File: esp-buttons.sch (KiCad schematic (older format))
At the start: 25 parts, among them Q1 FDV304P, U1 ESP-07v2, U2 LD1117S33CTR

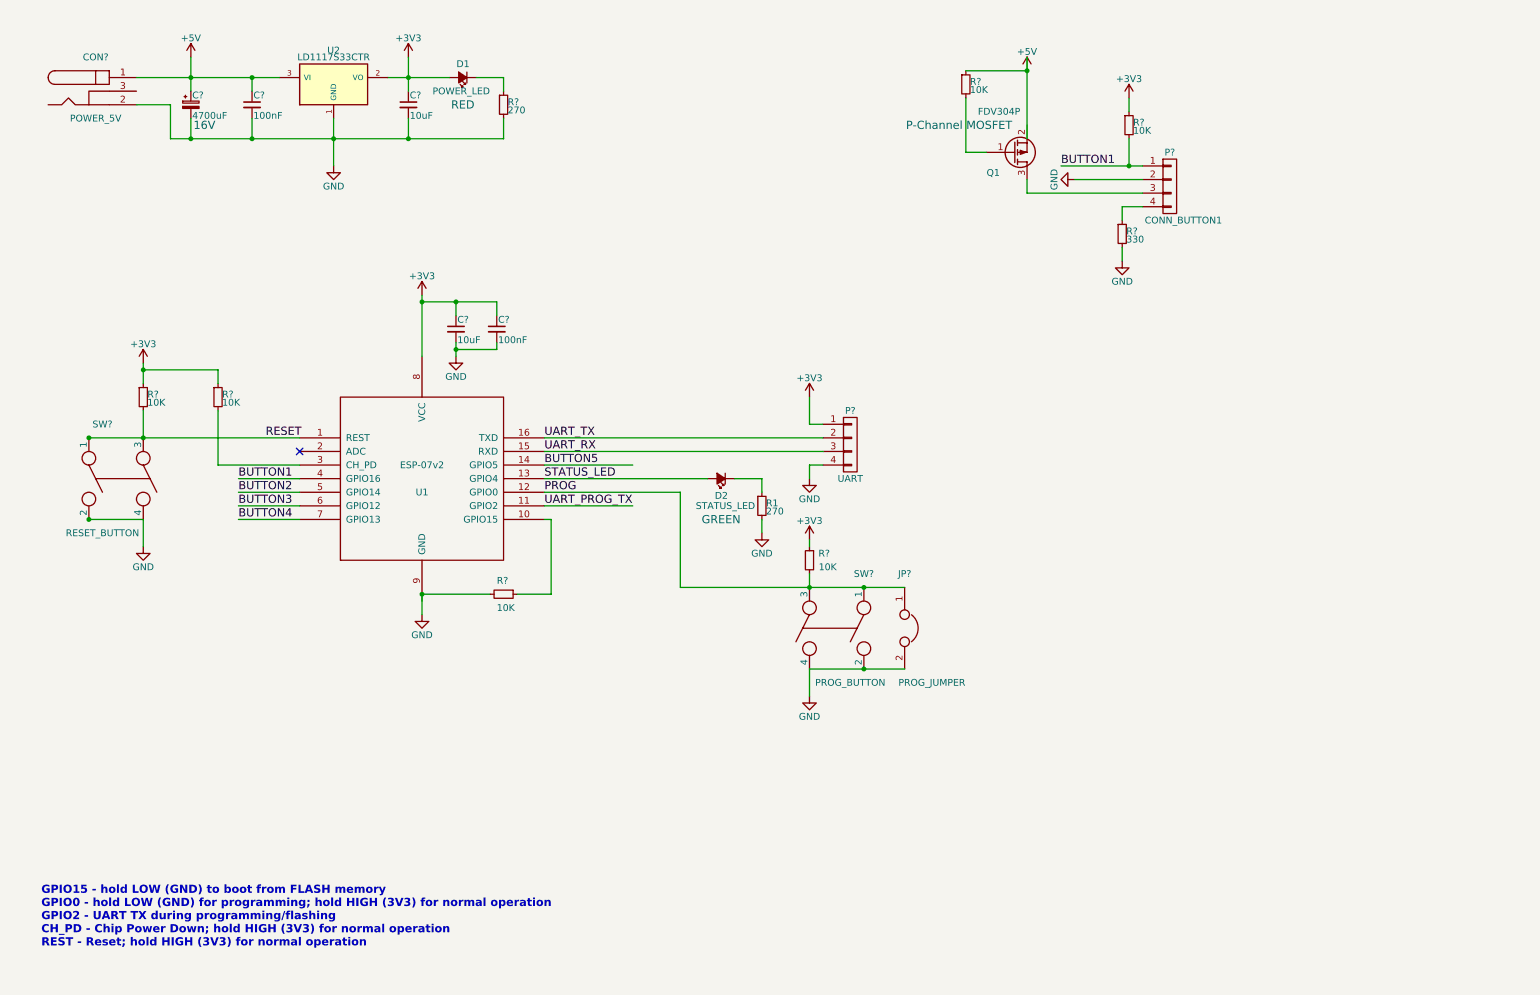
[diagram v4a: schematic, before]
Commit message: Added better circuit for BUTTON! & LED1
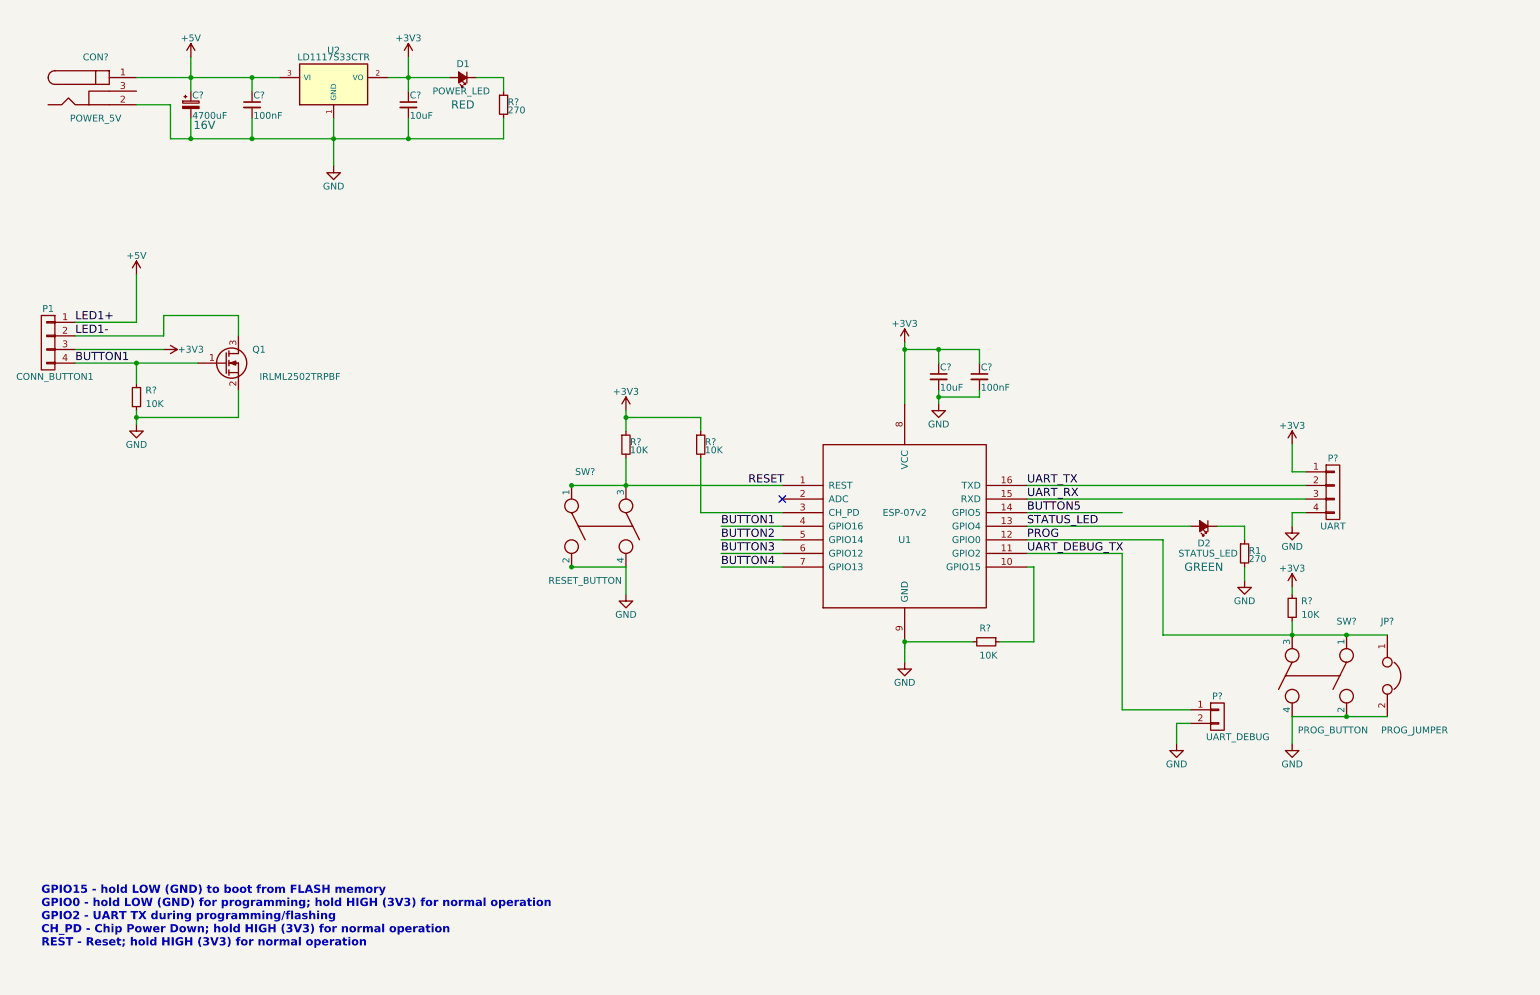
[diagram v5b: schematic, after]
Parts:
- removed Q1: FDV304P, TO_SOT_Packages_SMD:SOT-23, symbol Q_PMOS_GSD
- removed R?: 10K, Resistors_SMD:R_1206_HandSoldering, symbol R_Small
- removed R?: 330, Resistors_SMD:R_1206_HandSoldering, symbol R_Small
- added P?: UART_DEBUG, Pin_Headers:Pin_Header_Straight_1x02, symbol CONN_01X02
- added Q?: IRLML2502TRPBF, TO_SOT_Packages_SMD:SOT-23, symbol Q_NMOS_GSD
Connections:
- net labels added: LED1+, LED1-, UART_DEBUG_TX
- net labels removed: UART_PROG_TX
- wire segments 93 -> 75
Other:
- moved on the sheet: C?, D2, JP?, P1, P?, R1, R?, SW?, U1

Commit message: Added the rest of the buttons' circuits. Annotated the schematic
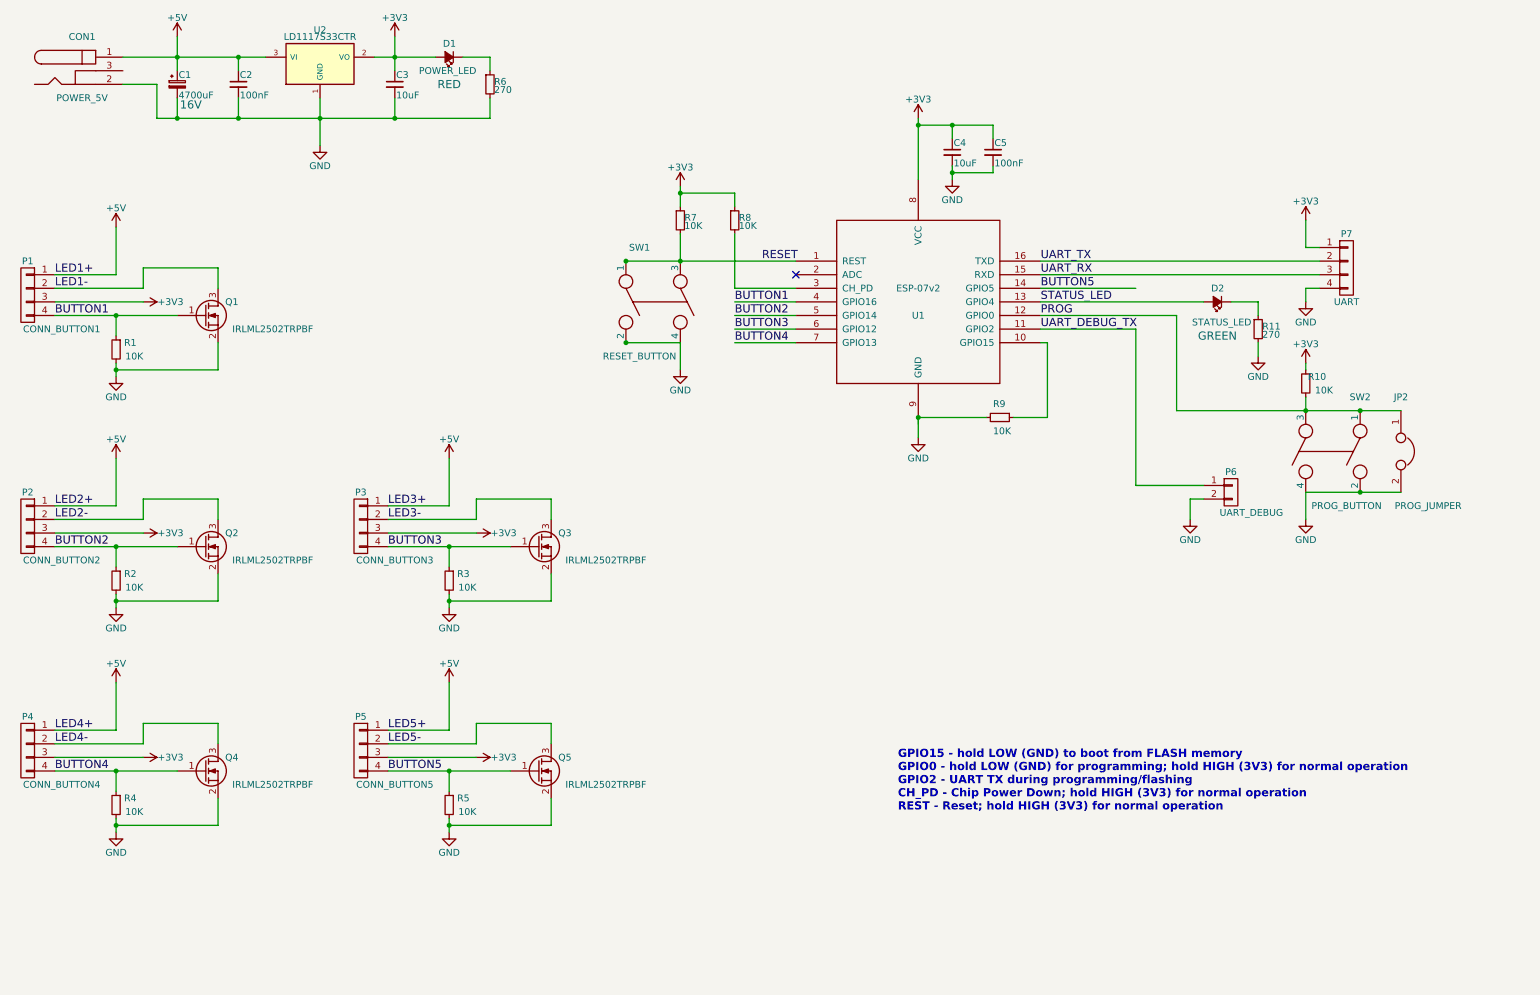
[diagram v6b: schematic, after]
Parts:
- added P2: CONN_BUTTON2, symbol CONN_01X04
- added P3: CONN_BUTTON3, symbol CONN_01X04
- added P4: CONN_BUTTON4, symbol CONN_01X04
- added P5: CONN_BUTTON5, symbol CONN_01X04
- added Q2, Q3, Q4, Q5: IRLML2502TRPBF, TO_SOT_Packages_SMD:SOT-23, symbol Q_NMOS_GSD
- added R2, R3, R4, R5: 10K, Resistors_SMD:R_1206_HandSoldering, symbol R_Small
- gave numbers to parts that had none: 19
- renumbered R1 to R11
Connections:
- net +3V3: now also P2.3 (P3), P3.3 (P3), P4.3 (P3), P5.3 (P3)
- net +5V: now also P2.1 (P1), P3.1 (P1), P4.1 (P1), P5.1 (P1)
- net BUTTON2: now also P2.4 (P4), Q2.1 (G), R2.1
- net BUTTON3: now also P3.4 (P4), Q3.1 (G), R3.1
- net BUTTON4: now also P4.4 (P4), Q4.1 (G), R4.1
- net BUTTON5: now also P5.4 (P4), Q5.1 (G), R5.1
- net GND: now also Q2.2 (S), Q3.2 (S), Q4.2 (S), Q5.2 (S), R2.2, R3.2, R4.2, R5.2
- new net LED2-: P2.2 (P2), Q2.3 (D)
- new net LED3-: P3.2 (P2), Q3.3 (D)
- new net LED4-: P4.2 (P2), Q4.3 (D)
- new net LED5-: P5.2 (P2), Q5.3 (D)
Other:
- moved on the sheet: C1, C2, C3, C4, C5, CON1, D1, D2, JP2, P1, P6, P7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

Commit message: Added circuit for USB-to-serial IC (FT230X). Added additional 5V power connector (terminal block connector)
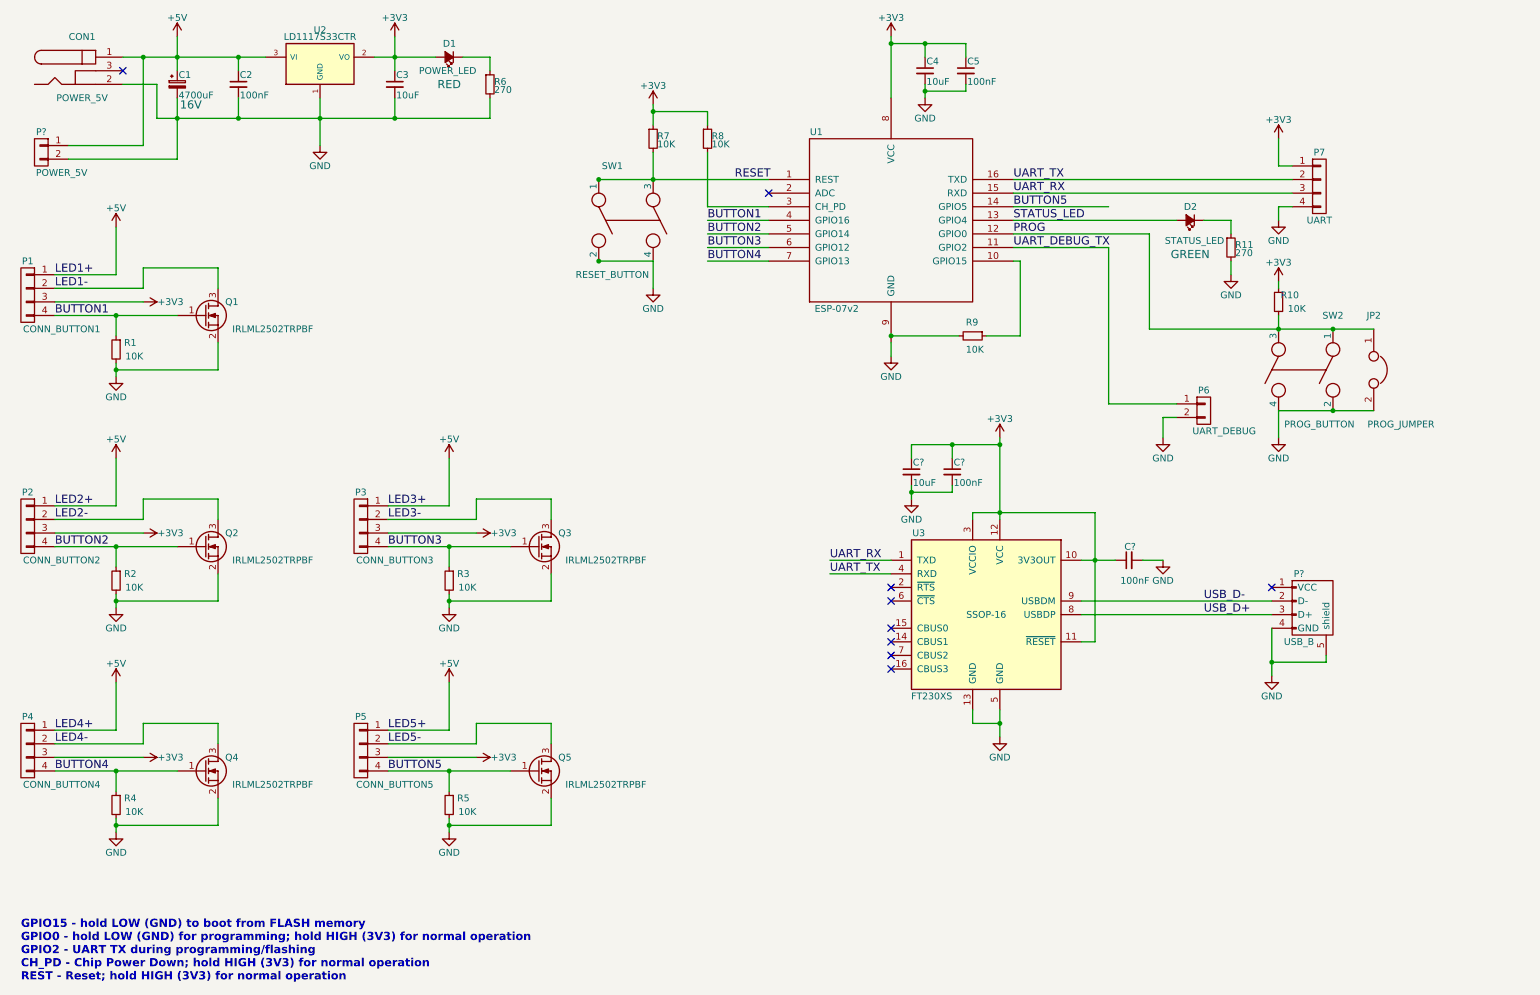
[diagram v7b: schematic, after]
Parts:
- added C?: 10uF, Capacitors_SMD:C_1210_HandSoldering, symbol C_Small
- added C? (x2): 100nF, Capacitors_SMD:C_1206_HandSoldering, symbol C_Small
- added P?: USB_B, Connect:USB_B, symbol USB_B
- added P?: POWER_5V, symbol CONN_01X02
- added U3: FT230XS, SSOP-16, symbol FT230XS
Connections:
- net +3V3: now also C?.1, C?.1, C?.1, U3.10 (3V3OUT), U3.11 (~RESET), U3.12 (VCC), U3.3 (VCCIO)
- net +5V: now also P?.1 (P1)
- net GND: now also U1.9 (GND), C?.2, C?.2, C?.2, P?.2 (P2), P?.4 (GND), P?.5 (shield), U3.13 (GND), U3.5 (GND); no longer R9.2
- net UART_RX: now also U3.1 (TXD)
- net UART_TX: now also U3.4 (RXD)
- new net USB_D+: P?.3 (D+), U3.8 (USBDP)
- new net USB_D-: P?.2 (D-), U3.9 (USBDM)
- no-connect marks 1 -> 9
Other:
- moved on the sheet: C4, C5, D2, JP2, P6, P7, R10, R11, R7, R8, R9, SW1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

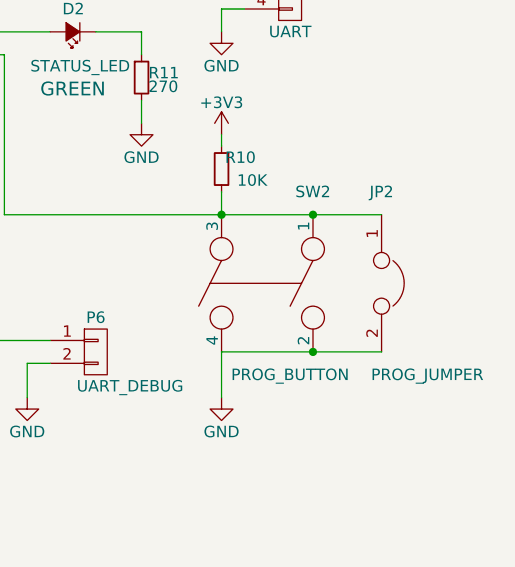
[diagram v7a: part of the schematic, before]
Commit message: Added temporary footprints to the button's connectors and the buttons
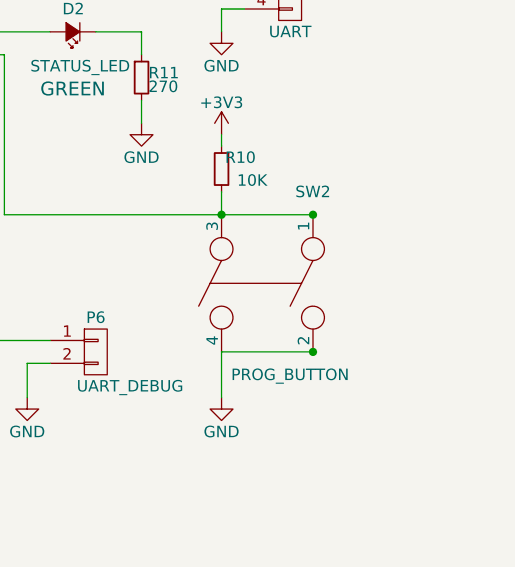
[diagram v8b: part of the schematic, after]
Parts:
- removed JP2: PROG_JUMPER, symbol JUMPER
- P1, P3, P4, P5: footprint (none) -> Terminal_Blocks:TerminalBlock_Pheonix_PT-3.5mm_4pol
- P2, P?: footprint (none) -> Terminal_Blocks:TerminalBlock_Pheonix_PT-3.5mm_2pol
- SW1: footprint (none) -> Buttons_Switches_SMD:SW_SPST_EVPBF
- SW2: footprint (none) -> Buttons_Switches_ThroughHole:SW_PUSH_6mm
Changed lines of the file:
@@
 F 0 "SW1" V 4600 2050 50  0000 C CNN
 F 1 "RESET_BUTTON" V 5400 2050 50  0000 C CNN
-F 2 "" H 5000 2150 50  0000 C CNN
+F 2 "Buttons_Switches_SMD:SW_SPST_EVPBF" H 5000 2150 50  0001 C CNN
 F 3 "" H 5000 2150 50  0000 C CNN
 	1    5000 2150
@@
 F 0 "P1" H 600 2950 50  0000 C CNN
 F 1 "CONN_BUTTON1" H 350 2450 50  0000 C CNN
-F 2 "" H 600 2700 50  0000 C CNN
+F 2 "Terminal_Blocks:TerminalBlock_Pheonix_PT-3.5mm_4pol" H 600 2700 50  0001 C CNN
 F 3 "" H 600 2700 50  0000 C CNN
 	1    600  2700
@@
 F 0 "SW2" V 9600 3050 50  0000 C CNN
 F 1 "PROG_BUTTON" V 10400 3150 50  0000 C CNN
-F 2 "" H 10000 3250 50  0000 C CNN
+F 2 "Buttons_Switches_ThroughHole:SW_PUSH_6mm" H 10000 3250 50  0001 C CNN
 F 3 "" H 10000 3250 50  0000 C CNN
 	1    10000 3250
@@
 Text Label 7850 2250 0    60   ~ 0
 PROG
-$Comp
-L JUMPER JP2
-U 1 1 57C84572
-P 10500 3250
-F 0 "JP2" V 10100 3250 50  0000 C CNN
-F 1 "PROG_JUMPER" V 10900 3450 50  0000 C CNN
-F 2 "" H 10500 3250 50  0000 C CNN
-F 3 "" H 10500 3250 50  0000 C CNN
-	1    10500 3250
-	0    1    1    0
-$EndComp
 Text Label 7850 2050 0    60   ~ 0
 BUTTON5
@@
 F 0 "P2" H 600 4650 50  0000 C CNN
 F 1 "CONN_BUTTON2" H 350 4150 50  0000 C CNN
-F 2 "" H 600 4400 50  0000 C CNN
+F 2 "Terminal_Blocks:TerminalBlock_Pheonix_PT-3.5mm_2pol" H 600 4400 50  0001 C CNN
 F 3 "" H 600 4400 50  0000 C CNN
 	1    600  4400
@@
 F 0 "P3" H 3050 4650 50  0000 C CNN
 F 1 "CONN_BUTTON3" H 2800 4150 50  0000 C CNN
-F 2 "" H 3050 4400 50  0000 C CNN
+F 2 "Terminal_Blocks:TerminalBlock_Pheonix_PT-3.5mm_4pol" H 3050 4400 50  0001 C CNN
 F 3 "" H 3050 4400 50  0000 C CNN
 	1    3050 4400
@@
 F 0 "P4" H 600 6300 50  0000 C CNN
 F 1 "CONN_BUTTON4" H 350 5800 50  0000 C CNN
-F 2 "" H 600 6050 50  0000 C CNN
+F 2 "Terminal_Blocks:TerminalBlock_Pheonix_PT-3.5mm_4pol" H 600 6050 50  0001 C CNN
 F 3 "" H 600 6050 50  0000 C CNN
 	1    600  6050
@@
 F 0 "P5" H 3050 6300 50  0000 C CNN
 F 1 "CONN_BUTTON5" H 2800 5800 50  0000 C CNN
-F 2 "" H 3050 6050 50  0000 C CNN
+F 2 "Terminal_Blocks:TerminalBlock_Pheonix_PT-3.5mm_4pol" H 3050 6050 50  0001 C CNN
 F 3 "" H 3050 6050 50  0000 C CNN
 	1    3050 6050
@@
 F 0 "P?" H 700 1800 50  0000 C CNN
 F 1 "POWER_5V" H 550 1500 50  0000 C CNN
-F 2 "" H 700 1650 50  0000 C CNN
+F 2 "Terminal_Blocks:TerminalBlock_Pheonix_PT-3.5mm_2pol" H 700 1650 50  0001 C CNN
 F 3 "" H 700 1650 50  0000 C CNN
 	1    700  1650
@@
 	9800 3550 10200 3550
 Wire Wire Line
-	10200 3550 10500 3550
-Wire Wire Line
 	9800 3550 9800 3750
 Connection ~ 9800 2950
@@
 	9800 2950 10200 2950
 Wire Wire Line
-	10200 2950 10500 2950
-Wire Wire Line
 	8850 2950 8850 2250
